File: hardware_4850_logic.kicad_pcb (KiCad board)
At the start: 4 copper layers, 84 x 79 mm, 201 parts, among them J101 PWM, J102 ADC, J1101 HALL, J1102 PWM_EN, J1103 CAN_IN, J1104 CAN_Out, J501 Enable, J601 AIN, J602 USB_B_Mini, J701 MOT_TEMP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

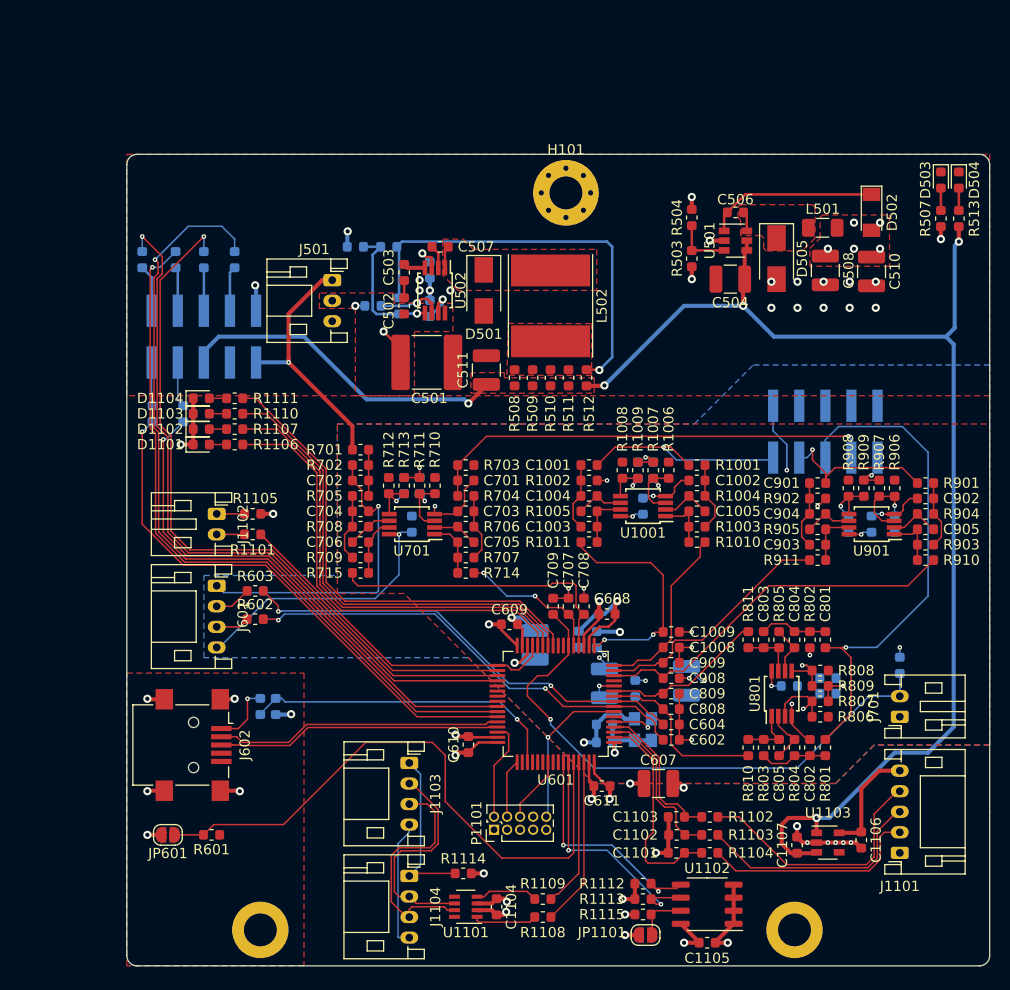
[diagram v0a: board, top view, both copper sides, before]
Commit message: made logic board leave bolt area
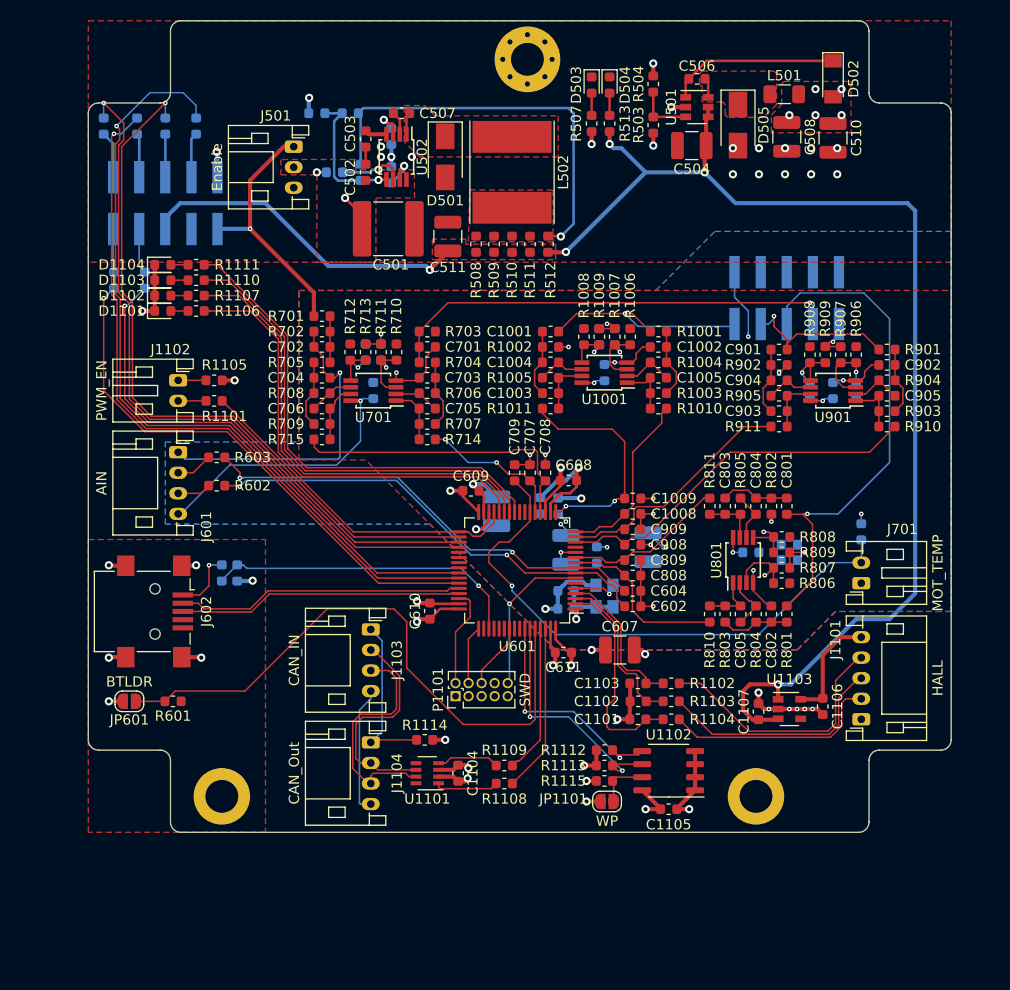
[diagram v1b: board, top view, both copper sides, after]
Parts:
- moved D503 35.2 mm to (151.2, 54.2)
- moved D504 35.2 mm to (153.0, 54.2)
- moved R507 35.2 mm to (151.2, 58.0)
- moved R513 35.2 mm to (153.0, 58.0)
- moved C504 13.5 mm to (161.0, 60.1)
- moved C506 13.5 mm to (161.5, 53.6)
- moved C510 13.5 mm to (174.8, 59.4)
- moved D502 13.5 mm to (174.8, 53.6)
- moved D505 13.5 mm to (165.5, 58.1)
- moved L501 13.5 mm to (170.0, 55.1)
- moved R503 13.5 mm to (157.2, 58.1)
- moved R504 13.5 mm to (157.2, 54.1)
- moved U501 13.5 mm to (161.5, 56.4)
- moved C1001 13.5 mm to (147.2, 78.2)
- moved C1002 13.5 mm to (157.8, 79.8)
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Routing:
- net (no net): track 2344.1 -> 2338.7 mm
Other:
- outline, holes or cut-outs redrawn

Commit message: Made gerbers ready to order
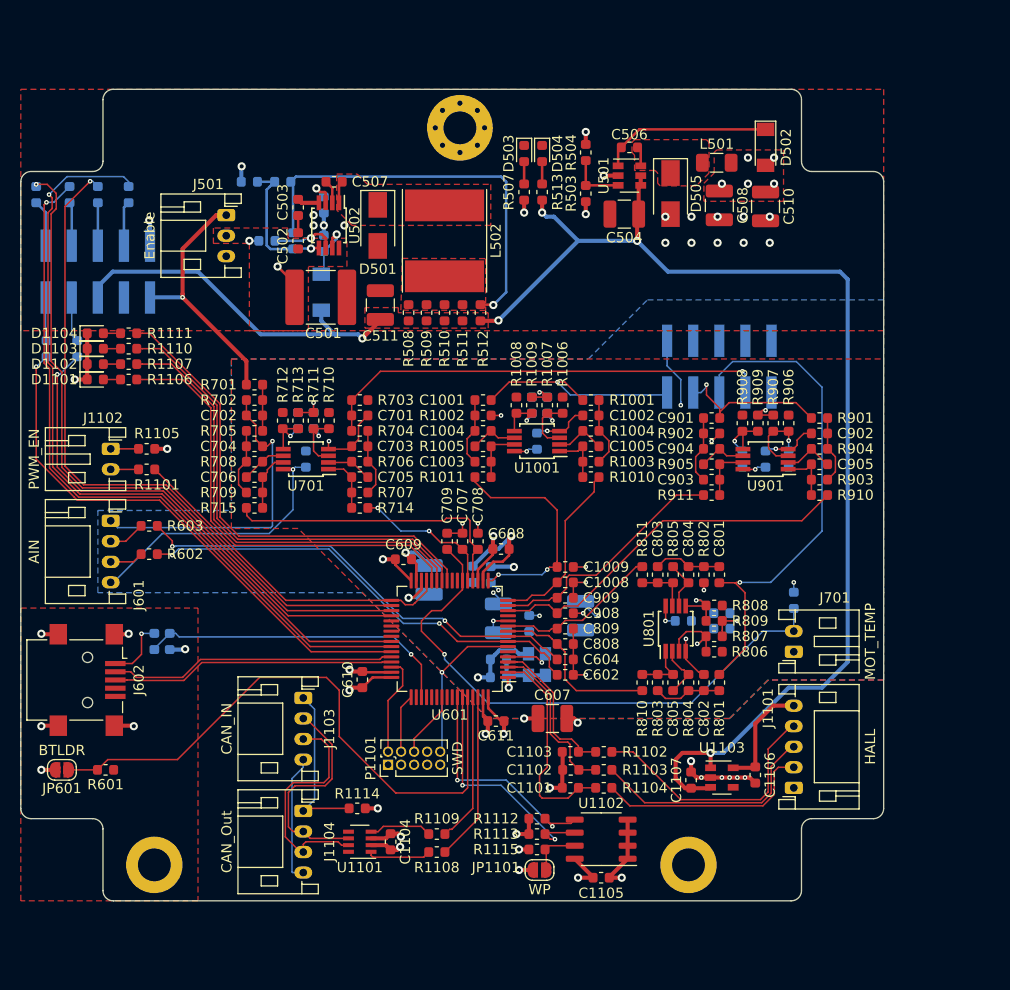
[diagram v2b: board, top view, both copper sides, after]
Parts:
- added D506: PMLL4153, Diode_SMD:D_MiniMELF, B.Cu at (124.9, 74.4)
- moved R501 9.36 mm to (119.6, 69.4)
- moved C1001 9.36 mm to (140.7, 84.9)
- moved C1002 9.36 mm to (151.2, 86.4)
- moved C1003 9.36 mm to (140.7, 90.9)
- moved C1004 9.36 mm to (140.7, 87.9)
- moved C1005 9.36 mm to (151.2, 89.4)
- moved C1006 9.36 mm to (146.9, 85.4)
- moved C1007 9.36 mm to (145.4, 85.4)
- moved C1008 9.36 mm to (148.7, 102.7)
- moved C1009 9.36 mm to (148.7, 101.2)
- moved C1010 9.36 mm to (145.9, 88.9)
- moved C1101 9.36 mm to (149.2, 122.7)
- moved C1102 9.36 mm to (149.2, 120.9)
- moved C1103 9.36 mm to (149.2, 119.2)
- moved C1104 9.36 mm to (131.7, 127.9)
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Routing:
- net (no net): track 2338.7 -> 2337.8 mm
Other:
- rule trace_min: 0.2 -> 0.15
